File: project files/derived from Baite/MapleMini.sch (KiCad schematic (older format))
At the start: 36 parts, among them J1 USB_C, J2 Left, J3 Right, Q1 BC817, Q2 BC817, SW1 Reset, SW2 Button, U1 STM32F103CBTx, U2 AMS1117-3.3, Y1 8MHz

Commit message: Coments on schematics
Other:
- note added: "Available schematics (supposingly of BAITE clones)\nuses MIC5219 and 2 individual SS14 diodes for both VBUS and Vin.\nThe boards I have utilize AMS117-33 and only one diode with S4 marking on it.\nThe AMS1117-33 on clones is coupled with 2 ceramic capacitors, \nwhile datasheet requires polar capacitors.\nS4 marking corresponds to SD103BWS Schottky barrier diode"
- note added: "Buttons & LED"
- note added: "Circuit for VCP over USB"
- note added: "Microcontroller core"
- note added: "Oscilator"
- note added: "Power management"
- note added: "Side connectors"
- note added: "USB type C as\nFull Speed USB 2.0"
- note removed: "Available schematics (supposingly of BAITE clones)\nuses MIC5219 and 2 individual SS14 diodes for both VBUS and Vin.\nThe boards I have utilize AMS117-33 and only one diode with S4 marking on it.\nS4 marking corresponds to SD103BWS Schottky barrier diode"
- note removed: "Garmonized with datasheet\nreference circuit"
- moved on the sheet: C5, C6, C7, C8, D2, J1, Q1, Q2, R1, R10, R11, R12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

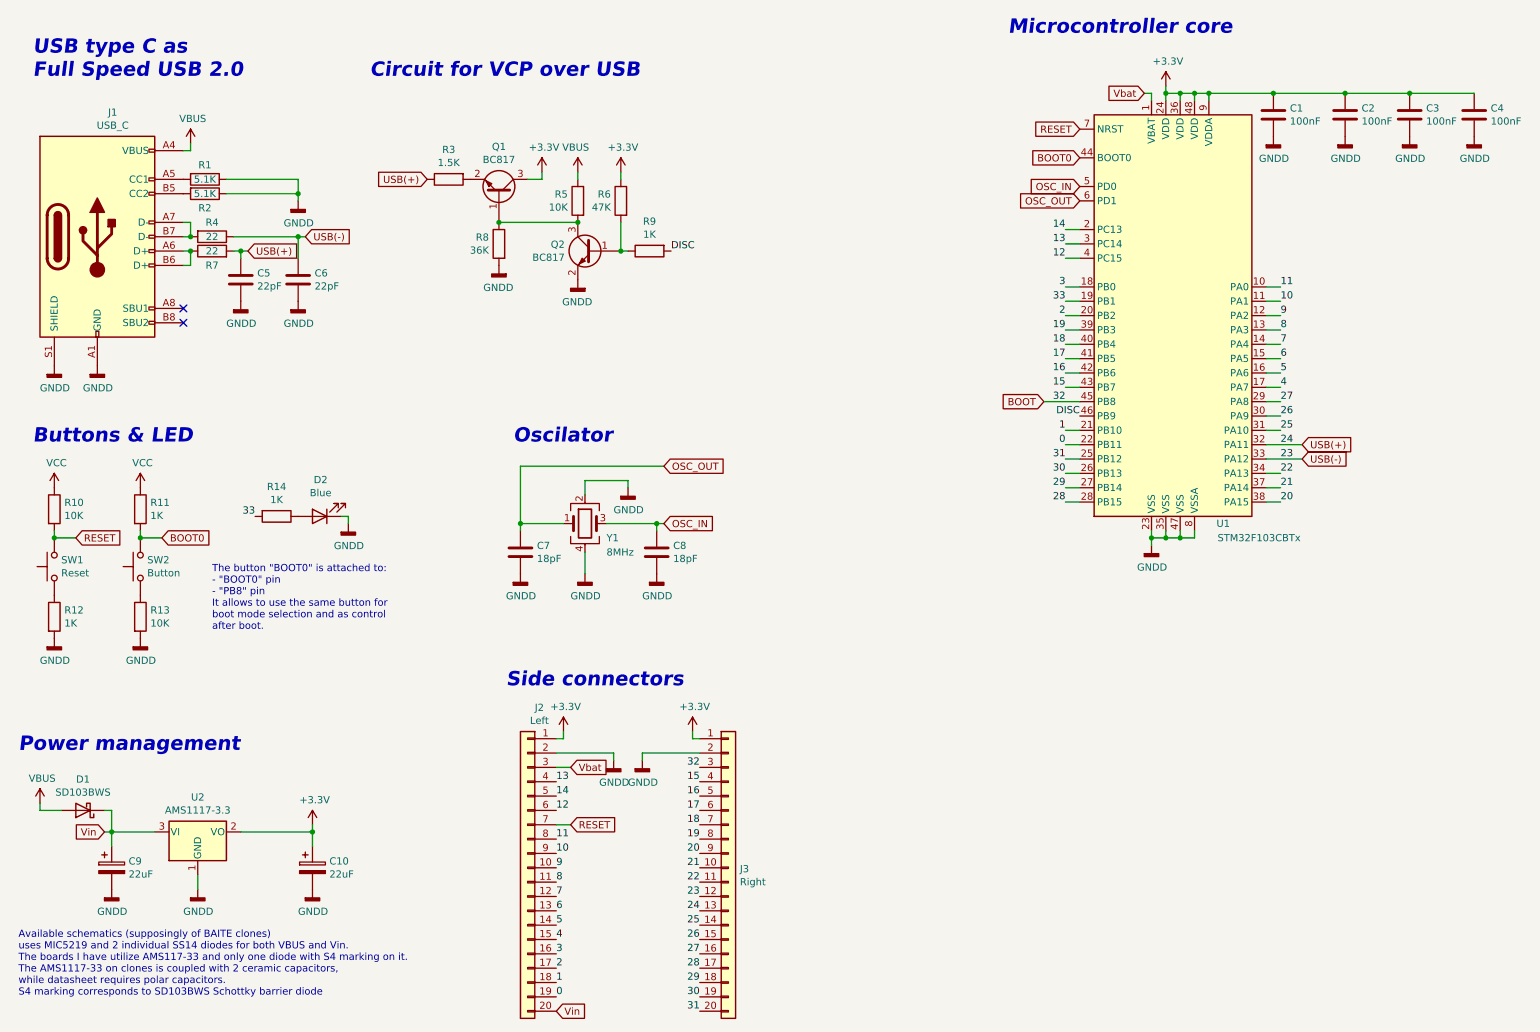
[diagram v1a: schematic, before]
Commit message: Added STDC connectors
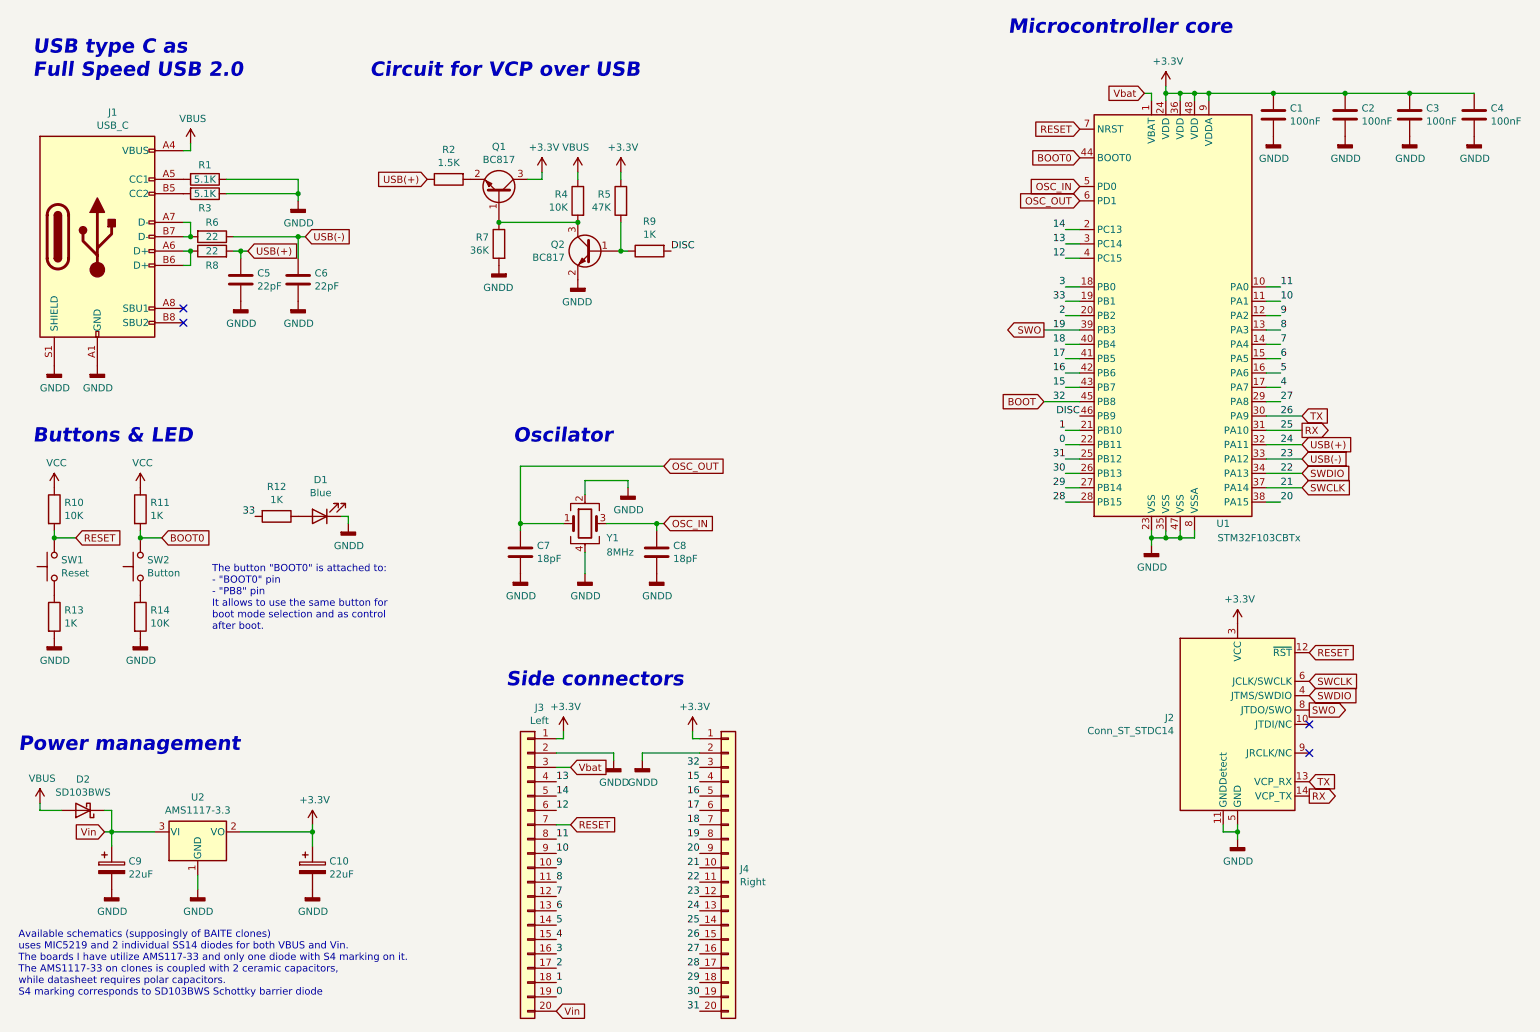
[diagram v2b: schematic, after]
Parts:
- added J2: Conn_ST_STDC14, Connector_PinHeader_1.27mm:PinHeader_2x07_P1.27mm_Vertical_SMD, symbol Connector:Conn_ST_STDC14
- renumbered D2 to D1, D1 to D2, J2 to J3, J3 to J4, R14 to R12, R12 to R13, R13 to R14, R3 to R2, R2 to R3, R5 to R4, R6 to R5, R4 to R6, R8 to R7, R7 to R8
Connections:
- net +3V3: now also J2.3 (VCC)
- net GNDD: now also J2.11 (GNDDetect), J2.5 (GND), J2.7 (GND)
- net RESET: now also J2.12 (~RST)
- net 19 renamed SWO
- net SWO: now also J2.8 (JTDO/SWO)
- net 21 renamed SWCLK
- net SWCLK: now also J2.6 (JCLK/SWCLK)
- net 22 renamed SWDIO
- net SWDIO: now also J2.4 (JTMS/SWDIO)
- net 25 renamed RX
- net RX: now also J2.14 (VCP_TX)
- net 26 renamed TX
- net TX: now also J2.13 (VCP_RX)
- no-connect marks 2 -> 4
